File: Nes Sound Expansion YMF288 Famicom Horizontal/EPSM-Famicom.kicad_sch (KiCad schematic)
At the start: 59 parts, among them J1 CARTRIDGE_F, J2 OUT_1, J3 EPSM_ADDRESSING, J4 CONSOLE_M, J5 AudioJack4_SwitchTR1, U1 74LS174, U10 74LS257, U2 74LS174, U3 74LS139, U4 74LS132, U5 YMF288, U6 BU9480F, U7 74LS257, U8 74LS257, U9 LM358, X1 SG-8002CA

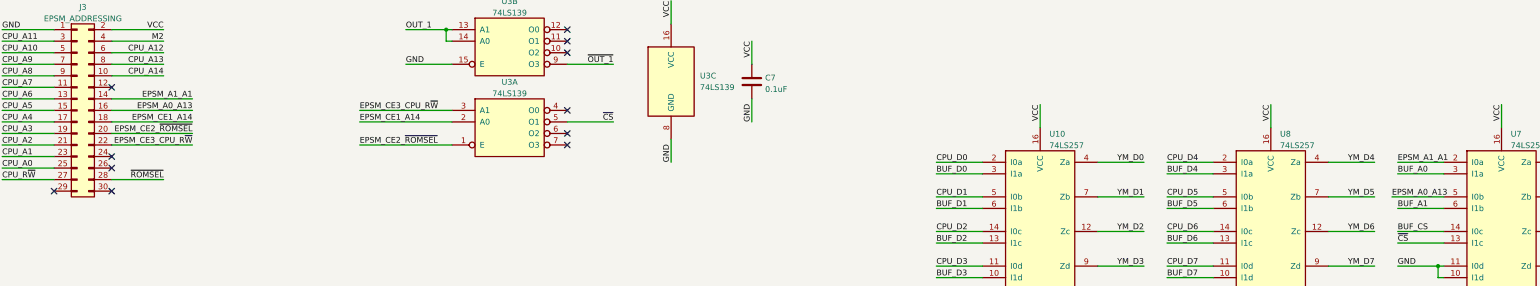
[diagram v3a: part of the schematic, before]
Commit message: Clarify EPSM chip enable and address net names
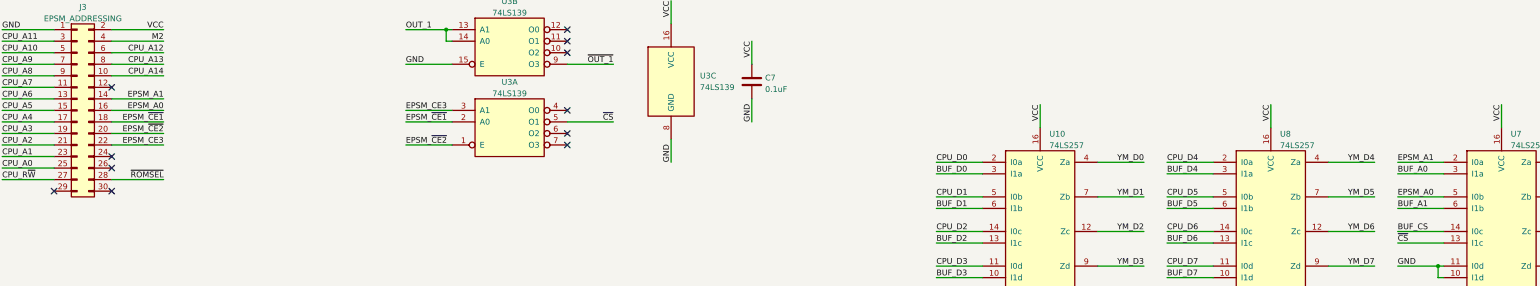
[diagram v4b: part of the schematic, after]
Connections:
- net EPSM_A0_A13 renamed EPSM_A0
- net EPSM_A1_A1 renamed EPSM_A1
- net EPSM_CE1_A14 renamed EPSM_~{CE1}
- net EPSM_CE2_~{ROMSEL} renamed EPSM_~{CE2}
- net EPSM_CE3_CPU_R~{W} renamed EPSM_CE3
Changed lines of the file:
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@@
+    (stroke (width 0) (type default) (color 0 0 0 0))
+  )
+  (wire (pts (xy 52.07 175.26) (xy 63.5 175.26))
     (stroke (width 0) (type default) (color 0 0 0 0))
   )
@@
     (stroke (width 0) (type default) (color 0 0 0 0))
   )
-  (wire (pts (xy 52.07 172.72) (xy 69.85 172.72))
+  (wire (pts (xy 52.07 172.72) (xy 63.5 172.72))
     (stroke (width 0) (type default) (color 0 0 0 0))
   )
@@
     (stroke (width 0) (type default) (color 0 0 0 0))
   )
-  (wire (pts (xy 106.68 170.18) (xy 127 170.18))
+  (wire (pts (xy 116.84 170.18) (xy 127 170.18))
     (stroke (width 0) (type default) (color 0 0 0 0))
   )
@@
     (stroke (width 0) (type default) (color 0 0 0 0))
   )
-  (wire (pts (xy 106.68 167.64) (xy 127 167.64))
+  (wire (pts (xy 116.84 167.64) (xy 127 167.64))
     (stroke (width 0) (type default) (color 0 0 0 0))
   )
@@
     (stroke (width 0) (type default) (color 0 0 0 0))
   )
-  (wire (pts (xy 52.07 165.1) (xy 69.85 165.1))
+  (wire (pts (xy 52.07 165.1) (xy 63.5 165.1))
     (stroke (width 0) (type default) (color 0 0 0 0))
   )
@@
     (stroke (width 0) (type default) (color 0 0 0 0))
   )
-  (wire (pts (xy 52.07 170.18) (xy 69.85 170.18))
+  (wire (pts (xy 52.07 170.18) (xy 63.5 170.18))
     (stroke (width 0) (type default) (color 0 0 0 0))
   )
@@
     (stroke (width 0) (type default) (color 0 0 0 0))
   )
-  (wire (pts (xy 334.01 186.69) (xy 345.44 186.69))
+  (wire (pts (xy 335.28 186.69) (xy 345.44 186.69))
     (stroke (width 0) (type default) (color 0 0 0 0))
   )
@@
     (stroke (width 0) (type default) (color 0 0 0 0))
   )
-  (wire (pts (xy 52.07 175.26) (xy 69.85 175.26))
-    (stroke (width 0) (type default) (color 0 0 0 0))
-  )
   (wire (pts (xy 106.68 49.53) (xy 118.11 49.53))
     (stroke (width 0) (type default) (color 0 0 0 0))
@@
     (stroke (width 0) (type default) (color 0 0 0 0))
   )
-  (wire (pts (xy 106.68 175.26) (xy 127 175.26))
+  (wire (pts (xy 116.84 175.26) (xy 127 175.26))
     (stroke (width 0) (type default) (color 0 0 0 0))
   )
@@
     (stroke (width 0) (type default) (color 0 0 0 0))
   )
-  (wire (pts (xy 52.07 167.64) (xy 69.85 167.64))
+  (wire (pts (xy 52.07 167.64) (xy 63.5 167.64))
     (stroke (width 0) (type default) (color 0 0 0 0))
   )
@@
     (effects (font (size 1.27 1.27)) (justify left bottom))
   )
-  (label "EPSM_A1_A1" (at 69.85 165.1 180)
+  (label "EPSM_A1" (at 63.5 165.1 180)
     (effects (font (size 1.27 1.27)) (justify right bottom))
   )
@@
     (effects (font (size 1.27 1.27)) (justify right bottom))
   )
-  (label "EPSM_CE3_CPU_R~{W}" (at 69.85 175.26 180)
-    (effects (font (size 1.27 1.27)) (justify right bottom))
-  )
   (label "YM_D0" (at 279.4 179.07 180)
     (effects (font (size 1.27 1.27)) (justify right bottom))
@@
     (effects (font (size 1.27 1.27)) (justify left bottom))
   )
-  (label "EPSM_A0_A13" (at 69.85 167.64 180)
+  (label "EPSM_A0" (at 63.5 167.64 180)
     (effects (font (size 1.27 1.27)) (justify right bottom))
   )
@@
     (effects (font (size 1.27 1.27)) (justify left bottom))
   )
-  (label "EPSM_CE2_~{ROMSEL}" (at 106.68 175.26 0)
-    (effects (font (size 1.27 1.27)) (justify left bottom))
-  )
   (label "VCC" (at 307.34 166.37 270)
     (effects (font (size 1.27 1.27)) (justify right bottom))
@@
     (effects (font (size 1.27 1.27)) (justify left bottom))
   )
+  (label "EPSM_~{CE2}" (at 116.84 175.26 0)
+    (effects (font (size 1.27 1.27)) (justify left bottom))
+  )
   (label "GND" (at 175.26 179.07 90)
     (effects (font (size 1.27 1.27)) (justify left bottom))
@@
     (effects (font (size 1.27 1.27)) (justify left bottom))
   )
-  (label "EPSM_A0_A13" (at 334.01 186.69 0)
+  (label "EPSM_A0" (at 335.28 186.69 0)
     (effects (font (size 1.27 1.27)) (justify left bottom))
   )
@@
     (effects (font (size 1.27 1.27)) (justify left bottom))
   )
-  (label "EPSM_CE1_A14" (at 69.85 170.18 180)
-    (effects (font (size 1.27 1.27)) (justify right bottom))
-  )
   (label "CPU_A14" (at 63.5 41.91 180)
     (effects (font (size 1.27 1.27)) (justify right bottom))
@@
     (effects (font (size 1.27 1.27)) (justify right bottom))
   )
-  (label "EPSM_CE1_A14" (at 106.68 170.18 0)
+  (label "EPSM_~{CE1}" (at 116.84 170.18 0)
     (effects (font (size 1.27 1.27)) (justify left bottom))
   )
@@
     (effects (font (size 1.27 1.27)) (justify left bottom))
   )
+  (label "EPSM_CE3" (at 63.5 175.26 180)
+    (effects (font (size 1.27 1.27)) (justify right bottom))
+  )
   (label "GND" (at 218.44 90.17 180)
     (effects (font (size 1.27 1.27)) (justify right bottom))
   )
-  (label "EPSM_A1_A1" (at 335.28 179.07 0)
+  (label "EPSM_A1" (at 335.28 179.07 0)
     (effects (font (size 1.27 1.27)) (justify left bottom))
   )
@@
     (effects (font (size 1.27 1.27)) (justify right bottom))
   )
-  (label "EPSM_CE3_CPU_R~{W}" (at 106.68 167.64 0)
+  (label "EPSM_CE3" (at 116.84 167.64 0)
     (effects (font (size 1.27 1.27)) (justify left bottom))
   )
@@
     (effects (font (size 1.27 1.27)) (justify left bottom))
   )
+  (label "EPSM_~{CE1}" (at 63.5 170.18 180)
+    (effects (font (size 1.27 1.27)) (justify right bottom))
+  )
   (label "PPU_D2" (at 82.55 100.33 0)
     (effects (font (size 1.27 1.27)) (justify left bottom))
@@
     (effects (font (size 1.27 1.27)) (justify right bottom))
   )
+  (label "EPSM_~{CE2}" (at 63.5 172.72 180)
+    (effects (font (size 1.27 1.27)) (justify right bottom))
+  )
   (label "VCC" (at 63.5 31.75 180)
     (effects (font (size 1.27 1.27)) (justify right bottom))
   )
-  (label "EPSM_CE2_~{ROMSEL}" (at 69.85 172.72 180)
-    (effects (font (size 1.27 1.27)) (justify right bottom))
-  )
